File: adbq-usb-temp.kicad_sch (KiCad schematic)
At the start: 74 parts, among them J4 USB_C_Receptacle_USB2.0_14P, Q1 Q_NMOS, Q2 Q_NMOS, Q3 Q_NMOS, SW1 SW_Push, SW2 TestPoint, SW3 TestPoint, SW4 TestPoint, U1 ESP32-S3FH4R2, U14 TMP117AIDRV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

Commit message: pcb: add production files
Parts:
- R1, R2, R24, R3, R57: JLCPCB Part # C25804 -> C25744; Manufacturer Part Number 0603WAF1002T5E -> 0402WGF1002TCE
- R12, R13: JLCPCB Part # C23186 -> C25905; Manufacturer Part Number 0603WAF5101T5E -> 0402WGF5101TCE
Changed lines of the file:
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@@
 			)
 		)
-		(property "JLCPCB Part #" "C25804"
+		(property "JLCPCB Part #" "C25744"
 			(at 55.88 74.93 0)
 			(effects
@@
 			)
 		)
-		(property "Manufacturer Part Number" "0603WAF1002T5E"
+		(property "Manufacturer Part Number" "0402WGF1002TCE"
 			(at 55.88 74.93 0)
 			(effects
@@
 			)
 		)
-		(property "Manufacturer Part Number" "0603WAF5101T5E"
+		(property "Manufacturer Part Number" "0402WGF5101TCE"
 			(at 46.99 143.51 90)
 			(effects
@@
 			)
 		)
-		(property "JLCPCB Part #" "C23186"
+		(property "JLCPCB Part #" "C25905"
 			(at 46.99 143.51 90)
 			(effects
@@
 			)
 		)
-		(property "Manufacturer Part Number" "0603WAF5101T5E"
+		(property "Manufacturer Part Number" "0402WGF5101TCE"
 			(at 46.99 140.97 90)
 			(effects
@@
 			)
 		)
-		(property "JLCPCB Part #" "C23186"
+		(property "JLCPCB Part #" "C25905"
 			(at 46.99 140.97 90)
 			(effects
@@
 			)
 		)
-		(property "JLCPCB Part #" "C25804"
+		(property "JLCPCB Part #" "C25744"
 			(at 247.65 129.54 0)
 			(effects
@@
 			)
 		)
-		(property "Manufacturer Part Number" "0603WAF1002T5E"
+		(property "Manufacturer Part Number" "0402WGF1002TCE"
 			(at 247.65 129.54 0)
 			(effects
@@
 			)
 		)
-		(property "JLCPCB Part #" "C25804"
+		(property "JLCPCB Part #" "C25744"
 			(at 146.05 64.77 90)
 			(effects
@@
 			)
 		)
-		(property "Manufacturer Part Number" "0603WAF1002T5E"
+		(property "Manufacturer Part Number" "0402WGF1002TCE"
 			(at 146.05 64.77 90)
 			(effects
@@
 			)
 		)
-		(property "JLCPCB Part #" "C25804"
+		(property "JLCPCB Part #" "C25744"
 			(at 55.88 29.21 0)
 			(effects
@@
 			)
 		)
-		(property "Manufacturer Part Number" "0603WAF1002T5E"
+		(property "Manufacturer Part Number" "0402WGF1002TCE"
 			(at 55.88 29.21 0)
 			(effects
@@
 			)
 		)
-		(property "JLCPCB Part #" "C25804"
+		(property "JLCPCB Part #" "C25744"
 			(at 241.3 72.39 90)
 			(effects
@@
 			)
 		)
-		(property "Manufacturer Part Number" "0603WAF1002T5E"
+		(property "Manufacturer Part Number" "0402WGF1002TCE"
 			(at 241.3 72.39 90)
 			(effects

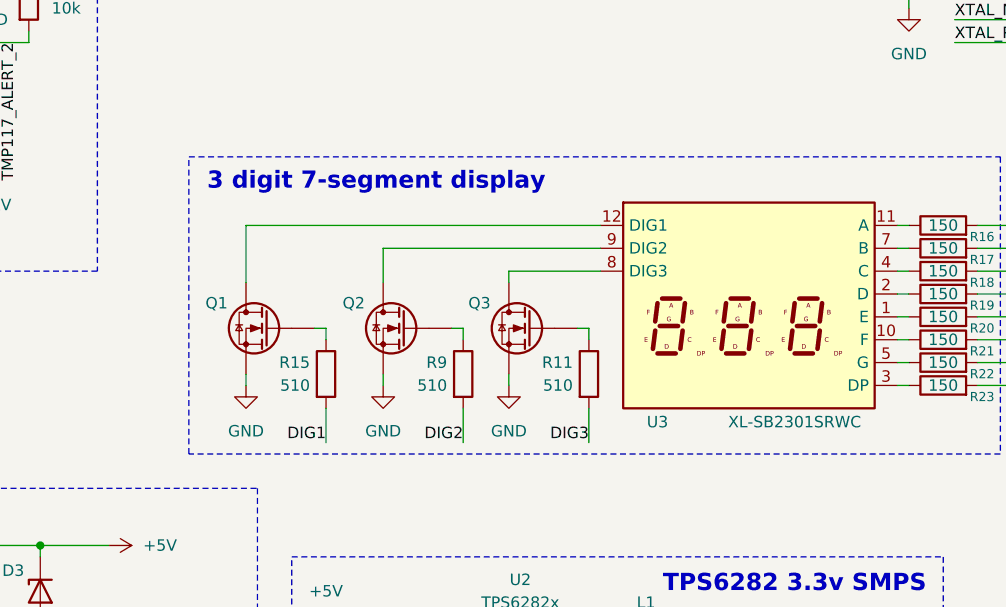
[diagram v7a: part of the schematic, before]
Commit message: schem: update segment display mosfets to correct led polarities
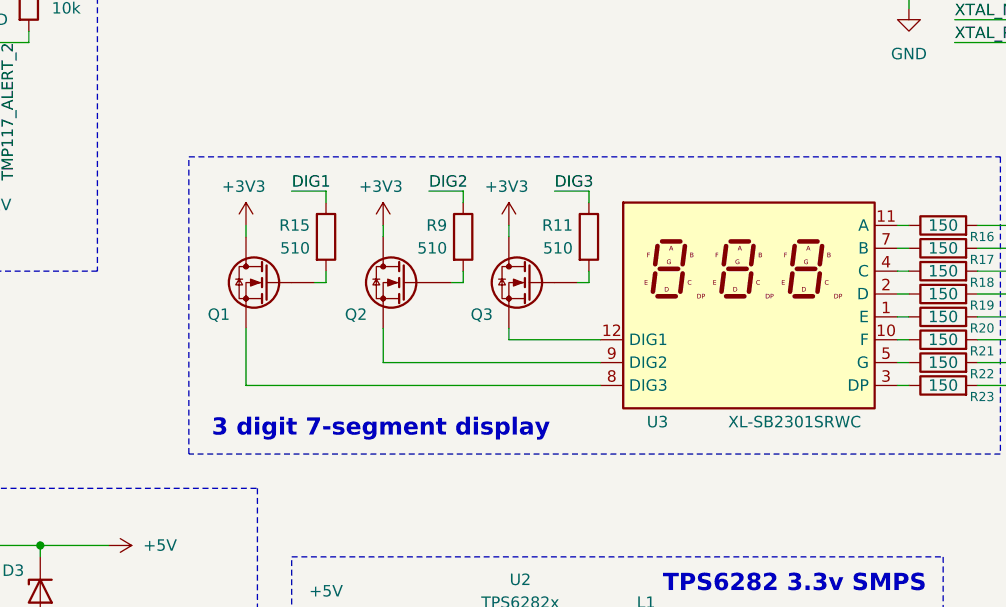
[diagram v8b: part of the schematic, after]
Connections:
- net +3V3: now also Q1.3 (D), Q2.3 (D), Q3.3 (D)
- net DIG1: now also R15.1; no longer R15.2
- net DIG2: now also R9.1; no longer R9.2
- net DIG3: now also R11.1; no longer R11.2
- net GND: no longer Q1.2 (S), Q2.2 (S), Q3.2 (S)
- net at Q1.1 (G): now also R15.2; no longer R15.1
- net at Q3.1 (G): now also R11.2; no longer R11.1
- net at U3.8 (DIG3): now also Q1.2 (S); no longer Q3.3 (D)
- net at U3.12 (DIG1): now also Q3.2 (S); no longer Q1.3 (D)
- net at Q2.1 (G): now also R9.2; no longer R9.1
- net at U3.9 (DIG2): now also Q2.2 (S); no longer Q2.3 (D)
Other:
- moved on the sheet: Q1, Q2, Q3, R11, R15, R9
